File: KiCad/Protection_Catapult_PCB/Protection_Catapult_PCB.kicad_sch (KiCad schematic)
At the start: 21 parts, among them J1 Motor_I, J2 Motor_D, J3 Control_D, J4 Control_I, J5 Alimentacion, J6 Alimentacion 5V, U1 A4988_STEPPER_MOTOR_DRIVER_CA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, U2 A4988_STEPPER_MOTOR_DRIVER_CA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, U3 DC_DC_small

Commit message: PCB Update.
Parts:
- added C1, C2: C, Capacitor_THT:C_Disc_D4.3mm_W1.9mm_P5.00mm, symbol Device:C
- added J10: Screw_Terminal_01x03, Connector_JST:JST_XH_B3B-XH-A_1x03_P2.50mm_Vertical, symbol Connector:Screw_Terminal_01x03
- added J11: Motor NEMA I, Connector_JST:JST_XH_B2B-XH-A_1x02_P2.50mm_Vertical, symbol Connector:Screw_Terminal_01x02
- added J12: Motor DC, Connector_JST:JST_XH_B2B-XH-A_1x02_P2.50mm_Vertical, symbol Connector:Screw_Terminal_01x02
- added J13: Motores 28BYJ-48, Connector_JST:JST_XH_B4B-XH-A_1x04_P2.50mm_Vertical, symbol Connector:Screw_Terminal_01x04
- added J15: Servo, Connector_JST:JST_XH_B1B-XH-AM_1x01_P2.50mm_Vertical, symbol Connector:Screw_Terminal_01x01
- added J16: Motor NEMA D, Connector_JST:JST_XH_B2B-XH-A_1x02_P2.50mm_Vertical, symbol Connector:Screw_Terminal_01x02
- added J17: Alimentacion L298N, Connectors_Terminal_Blocks_SID:TerminalBlock_Pheonix_MPT-2.54mm_2pol, symbol Connector:Screw_Terminal_01x02
- added J7, J8: Screw_Terminal_01x05, Connector_JST:JST_XH_B5B-XH-A_1x05_P2.50mm_Vertical, symbol Connector:Screw_Terminal_01x05
- added J9: Screw_Terminal_01x04, Connector_JST:JST_XH_B4B-XH-A_1x04_P2.50mm_Vertical, symbol Connector:Screw_Terminal_01x04
- added U4, U5: ULN2003A, Package_DIP:CERDIP-16_W7.62mm_SideBrazed, symbol Transistor_Array:ULN2003A
- added U6: ESP32-S3-DevKitC, PCM_Espressif:ESP32-S3-DevKitC, symbol PCM_Espressif:ESP32-S3-DevKitC
- U3: footprint DC_DC_LM2596_small:DC_DC_LM2596_small -> DC_DC_LM2596_small:DC_DC_LM2596_small
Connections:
- net +12V: now also C1.2, C2.2, J17.1 (Pin_1), J7.5 (Pin_5), J8.5 (Pin_5), U4.9 (COM), U5.9 (COM)
- net +5V: now also J10.2 (Pin_2), U6.1 (3V3), U6.2 (3V3)
- net GND: now also C1.1, C2.1, J10.3 (Pin_3), J17.2 (Pin_2), U4.8 (GND), U5.8 (GND), U6.22 (GND), U6.23 (GND), U6.24 (GND), U6.44 (GND)
- new net: J7.1 (Pin_1), U4.13 (O4)
- new net: J7.2 (Pin_2), U4.14 (O3)
- new net: J7.3 (Pin_3), U4.15 (O2)
- new net: J7.4 (Pin_4), U4.16 (O1)
- new net: J11.1 (Pin_1), U6.12 (GPIO8/ADC1_CH7)
- new net: J13.4 (Pin_4), U6.13 (GPIO3/ADC1_CH2)
- new net: J16.2 (Pin_2), U6.15 (GPIO9/ADC1_CH8)
- new net: J16.1 (Pin_1), U6.16 (GPIO10/ADC1_CH9)
- new net: J15.1 (Pin_1), U6.17 (GPIO11/ADC2_CH0)
- new net: J12.2 (Pin_2), U6.18 (GPIO12/ADC2_CH1)
- new net: J12.1 (Pin_1), U6.19 (GPIO13/ADC2_CH2)
- new net: J13.3 (Pin_3), U6.4 (GPIO4/ADC1_CH3)
- new net: J13.2 (Pin_2), U6.5 (GPIO5/ADC1_CH4)
- new net: J13.1 (Pin_1), U6.6 (GPIO6/ADC1_CH5)
- new net: J11.2 (Pin_2), U6.7 (GPIO7/ADC1_CH6)
- new net: J8.1 (Pin_1), U5.10 (O7)
- new net: J8.2 (Pin_2), U5.11 (O6)
- new net: J8.3 (Pin_3), U5.12 (O5)
- new net: J8.4 (Pin_4), U5.13 (O4)
- new net In1: J9.4 (Pin_4), U4.1 (I1), U5.7 (I7)
- new net In2: J9.3 (Pin_3), U4.2 (I2), U5.6 (I6)
- new net In3: J9.2 (Pin_2), U4.3 (I3), U5.5 (I5)
- new net In4: J9.1 (Pin_1), U4.4 (I4), U5.4 (I4)
- new net Servo: J10.1 (Pin_1)
- no-connect marks 2 -> 8

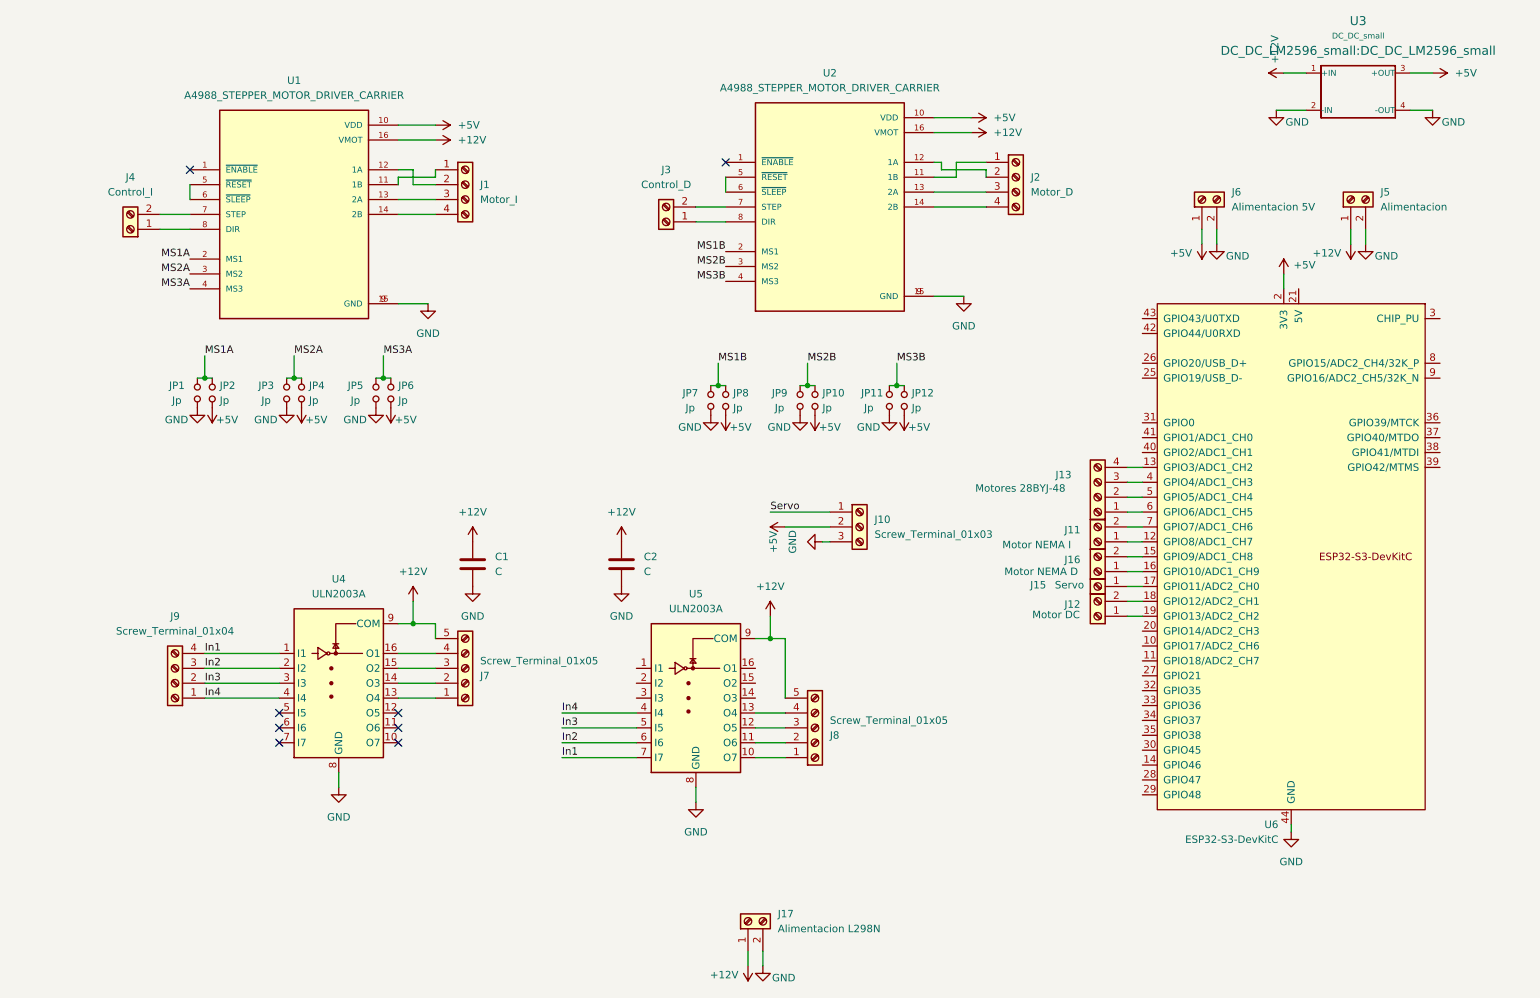
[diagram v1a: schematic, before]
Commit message: NEMA 17 supports added.
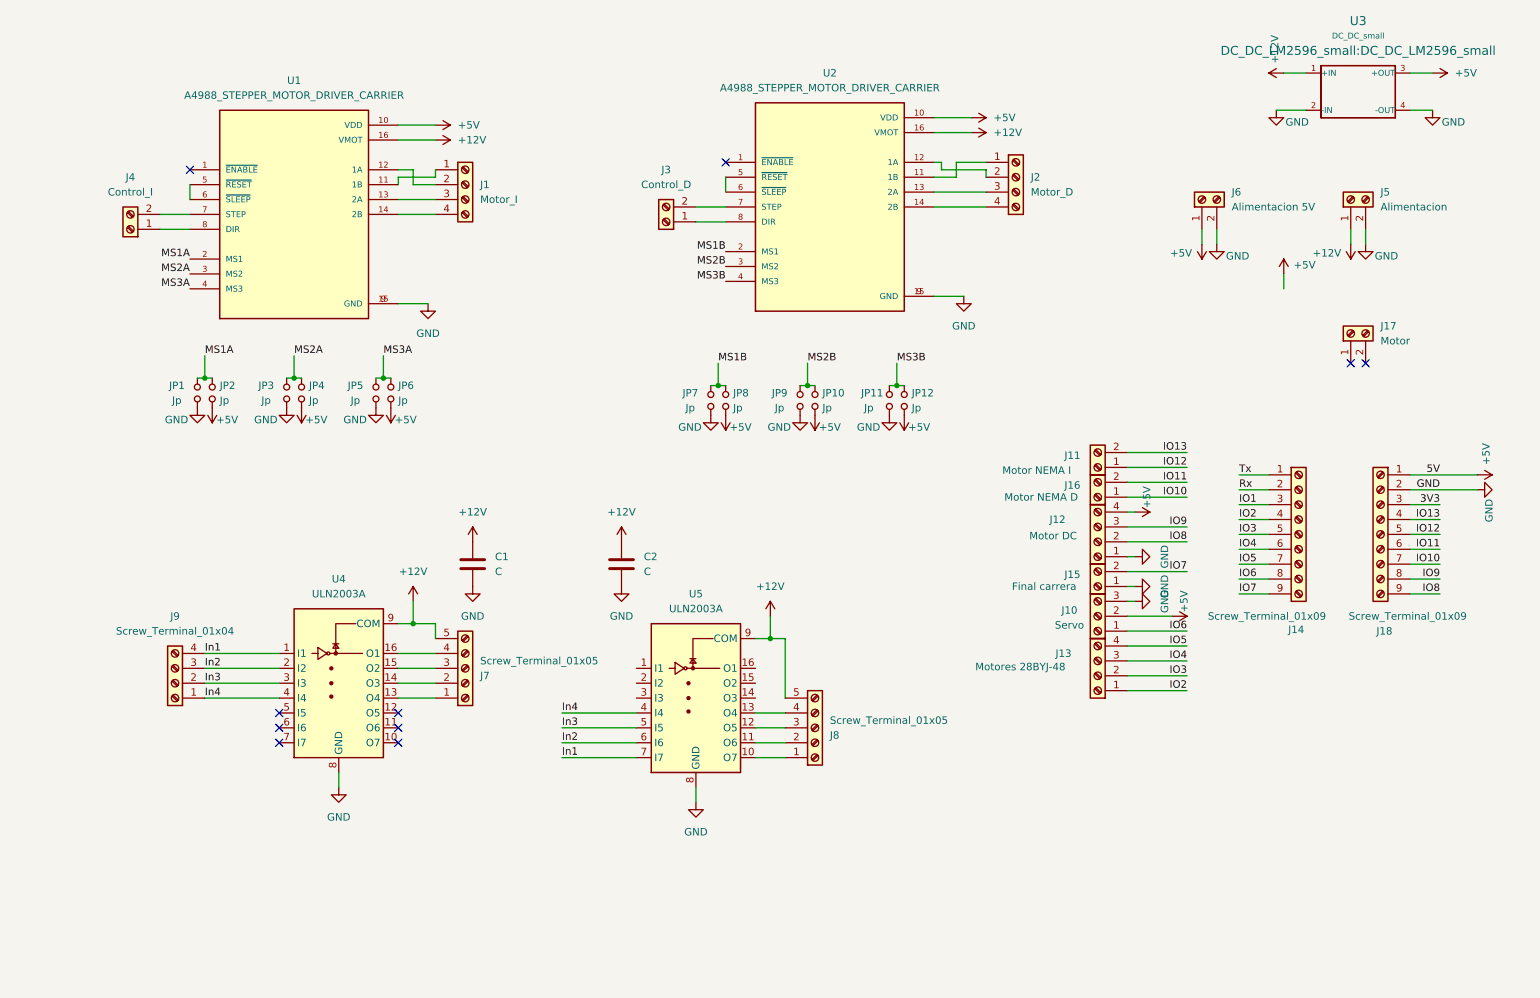
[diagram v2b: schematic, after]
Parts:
- removed J12: Motor DC, Connector_JST:JST_XH_B2B-XH-A_1x02_P2.50mm_Vertical, symbol Connector:Screw_Terminal_01x02
- removed J15: Servo, Connector_JST:JST_XH_B1B-XH-AM_1x01_P2.50mm_Vertical, symbol Connector:Screw_Terminal_01x01
- removed U6: ESP32-S3-DevKitC, PCM_Espressif:ESP32-S3-DevKitC, symbol PCM_Espressif:ESP32-S3-DevKitC
- added J12: Motor DC, Connector_JST:JST_XH_B4B-XH-A_1x04_P2.50mm_Vertical, symbol Connector:Screw_Terminal_01x04
- added J14, J18: Screw_Terminal_01x09, Connector_PinHeader_2.54mm:PinHeader_1x09_P2.54mm_Vertical, symbol Connector:Screw_Terminal_01x09
- added J15: Final carrera, Connector_JST:JST_XH_B2B-XH-A_1x02_P2.50mm_Vertical, symbol Connector:Screw_Terminal_01x02
- J10: value Screw_Terminal_01x03 -> Servo
- J17: value Alimentacion L298N -> Motor; footprint Connectors_Terminal_Blocks_SID:TerminalBlock_Pheonix_MPT-2.54mm_2pol -> Connector_JST:JST_XH_B2B-XH-A_1x02_P2.50mm_Vertical
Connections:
- net +12V: no longer J17.1 (Pin_1)
- net +5V: now also J12.4 (Pin_4), J18.1 (Pin_1)
- net GND: now also J12.1 (Pin_1), J15.1 (Pin_1), J18.2 (Pin_2); no longer J17.2 (Pin_2)
- net IO12: now reaches J11.1 (Pin_1)
- net IO12: now also J18.5 (Pin_5)
- net IO5: now reaches J13.4 (Pin_4)
- net IO5: now also J14.7 (Pin_7)
- net IO11: now reaches J16.2 (Pin_2)
- net IO11: now also J18.6 (Pin_6)
- net IO10: now reaches J16.1 (Pin_1)
- net IO10: now also J18.7 (Pin_7)
- net IO4: now reaches J13.3 (Pin_3)
- net IO4: now also J14.6 (Pin_6)
- net IO3: now reaches J13.2 (Pin_2)
- net IO3: now also J14.5 (Pin_5)
- net IO2: now reaches J13.1 (Pin_1)
- net IO2: now also J14.4 (Pin_4)
- net IO13: now reaches J11.2 (Pin_2)
- net IO13: now also J18.4 (Pin_4)
- net Servo renamed IO6
- net IO6: now also J14.8 (Pin_8)
- new net 3V3: J18.3 (Pin_3)
- new net IO1: J14.3 (Pin_3)
- new net IO7: J14.9 (Pin_9), J15.2 (Pin_2)
- new net IO8: J12.2 (Pin_2), J18.9 (Pin_9)
- new net IO9: J12.3 (Pin_3), J18.8 (Pin_8)
- new net Rx: J14.2 (Pin_2)
- new net Tx: J14.1 (Pin_1)
- no-connect marks 8 -> 10
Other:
- moved on the sheet: J10, J11, J13, J16

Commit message: Enable for A4988 PCB update toi disconect the motors.
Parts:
- added J19, J20: Screw_Terminal_01x01, Connector_PinHeader_2.54mm:PinHeader_1x01_P2.54mm_Vertical, symbol Connector:Screw_Terminal_01x01
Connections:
- net IO1: now also J20.1 (Pin_1)
- net Enable: now reaches U2.1 (~{ENABLE})
- net Enable: now also U1.1 (~{ENABLE}), J19.1 (Pin_1)
- no-connect marks 10 -> 8
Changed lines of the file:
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@@
 	)
 	(no_connect
-		(at 59.69 46.99)
-	)
-	(no_connect
 		(at 257.81 80.01)
 	)
@@
 	)
 	(no_connect
-		(at 151.13 45.72)
-	)
-	(no_connect
 		(at 95.25 142.24)
 	)
@@
 	(wire
 		(pts
+			(xy 140.97 45.72) (xy 151.13 45.72)
+		)
+		(stroke
+			(width 0)
+			(type default)
+		)
+	)
+	(wire
+		(pts
 			(xy 101.6 127) (xy 101.6 124.46)
 		)
@@
 	(wire
 		(pts
+			(xy 46.99 46.99) (xy 59.69 46.99)
+		)
+		(stroke
+			(width 0)
+			(type default)
+		)
+	)
+	(wire
+		(pts
 			(xy 267.97 104.14) (xy 273.05 104.14)
 		)
@@
 	(wire
 		(pts
+			(xy 219.71 138.43) (xy 229.87 138.43)
+		)
+		(stroke
+			(width 0)
+			(type default)
+		)
+	)
+	(wire
+		(pts
 			(xy 62.23 132.08) (xy 74.93 132.08)
 		)
@@
 		)
 	)
+	(label "IO1"
+		(at 229.87 138.43 180)
+		(fields_autoplaced yes)
+		(effects
+			(font
+				(size 1.27 1.27)
+			)
+			(justify right bottom)
+		)
+	)
 	(label "MS2A"
 		(at 59.69 64.77 180)
@@
 		)
 	)
+	(label "Enable"
+		(at 53.34 46.99 0)
+		(fields_autoplaced yes)
+		(effects
+			(font
+				(size 1.27 1.27)
+			)
+			(justify left bottom)
+		)
+	)
 	(label "GND"
 		(at 273.05 101.6 180)
@@
 		)
 	)
+	(label "Enable"
+		(at 140.97 45.72 0)
+		(fields_autoplaced yes)
+		(effects
+			(font
+				(size 1.27 1.27)
+			)
+			(justify left bottom)
+		)
+	)
 	(label "IO12"
 		(at 273.05 109.22 180)
@@
 	)
 	(symbol
+		(lib_id "Connector:Screw_Terminal_01x01")
+		(at 41.91 46.99 180)
+		(unit 1)
+		(exclude_from_sim no)
+		(in_bom yes)
+		(on_board yes)
+		(dnp no)
+		(fields_autoplaced yes)
+		(property "Reference" "J19"
+			(at 41.91 40.64 0)
+			(effects
+				(font
+					(size 1.27 1.27)
+				)
+			)
+		)
+		(property "Value" "Screw_Terminal_01x01"
+			(at 41.91 43.18 0)
+			(effects
+				(font
+					(size 1.27 1.27)
+				)
+			)
+		)
+		(property "Footprint" "Connector_PinHeader_2.54mm:PinHeader_1x01_P2.54mm_Vertical"
+			(at 41.91 46.99 0)
+			(effects
+				(font
+					(size 1.27 1.27)
+				)
+				(hide yes)
+			)
+		)
+		(property "Datasheet" "~"
+			(at 41.91 46.99 0)
+			(effects
+				(font
+					(size 1.27 1.27)
+				)
+				(hide yes)
+			)
+		)
+		(property "Description" "Generic screw terminal, single row, 01x01, script generated (kicad-library-utils/schlib/autogen/connector/)"
+			(at 41.91 46.99 0)
+			(effects
+				(font
+					(size 1.27 1.27)
+				)
+				(hide yes)
+			)
+		)
+		(pin "1"
+		)
+		(instances
+			(project "Protection_Catapult_PCB"
+				(path "/8fcbbe2d-cf52-4bcc-a0da-099ebd3c8b8f"
+					(reference "J19")
+					(unit 1)
+				)
+			)
+		)
+	)
+	(symbol
 		(lib_id "Connector:Screw_Terminal_01x09")
 		(at 262.89 109.22 0)
@@
 		)
 		(instances
-			(project ""
+			(project "Protection_Catapult_PCB"
 				(path "/8fcbbe2d-cf52-4bcc-a0da-099ebd3c8b8f"
 					(reference "J10")
@@
 	)
 	(symbol
+		(lib_id "Connector:Screw_Terminal_01x01")
+		(at 214.63 138.43 180)
+		(unit 1)
+		(exclude_from_sim no)
+		(in_bom yes)
+		(on_board yes)
+		(dnp no)
+		(property "Reference" "J20"
+			(at 203.962 135.89 0)
+			(effects
+				(font
+					(size 1.27 1.27)
+				)
+			)
+		)
+		(property "Value" "Screw_Terminal_01x01"
+			(at 201.93 138.176 0)
+			(effects
+				(font
+					(size 1.27 1.27)
+				)
+			)
+		)
+		(property "Footprint" "Connector_PinHeader_2.54mm:PinHeader_1x01_P2.54mm_Vertical"
+			(at 214.63 138.43 0)
+			(effects
+				(font
+					(size 1.27 1.27)
+				)
+				(hide yes)
+			)
+		)
+		(property "Datasheet" "~"
+			(at 214.63 138.43 0)
+			(effects
+				(font
+					(size 1.27 1.27)
+				)
+				(hide yes)
+			)
+		)
+		(property "Description" "Generic screw terminal, single row, 01x01, script generated (kicad-library-utils/schlib/autogen/connector/)"
+			(at 214.63 138.43 0)
+			(effects
+				(font
+					(size 1.27 1.27)
+				)
+				(hide yes)
+			)
+		)
+		(pin "1"
+		)
+		(instances
+			(project "Protection_Catapult_PCB"
+				(path "/8fcbbe2d-cf52-4bcc-a0da-099ebd3c8b8f"
+					(reference "J20")
+					(unit 1)
+				)
+			)
+		)
+	)
+	(symbol
 		(lib_id "A4988_STEPPER_MOTOR_DRIVER_CARRIER:A4988_STEPPER_MOTOR_DRIVER_CARRIER")
 		(at 77.47 54.61 0)
@@
 		)
 		(instances
-			(project ""
+			(project "Protection_Catapult_PCB"
 				(path "/8fcbbe2d-cf52-4bcc-a0da-099ebd3c8b8f"
 					(reference "C1")
@@
 		)
 		(instances
-			(project ""
+			(project "Protection_Catapult_PCB"
 				(path "/8fcbbe2d-cf52-4bcc-a0da-099ebd3c8b8f"
 					(reference "J14")
@@
 		)
 		(instances
-			(project ""
+			(project "Protection_Catapult_PCB"
 				(path "/8fcbbe2d-cf52-4bcc-a0da-099ebd3c8b8f"
 					(reference "U4")
